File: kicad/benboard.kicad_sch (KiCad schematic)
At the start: 58 parts, among them J1 USB_C_Receptacle_USB2.0, SW1 SW_Push, U1 nRF52840, U2 BQ24075RGT, Y1 32MHz, Y2 32.768kHz

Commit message: more cad files as well as readme
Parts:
- added J2: ~, symbol vik:vik-keyboard-connector
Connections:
- net GND: now also J2.2 (GND)
- net VBUS: now also J2.6 (5V)
- net VDD_NRF: now also J2.1 (3V3)
- no-connect marks 6 -> 7
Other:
- note added: "VIK"
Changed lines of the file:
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@@
   (no_connect (at 270.51 73.66))
   (no_connect (at 64.77 77.47))
+  (no_connect (at 177.8 190.5))
   (no_connect (at 171.45 62.23))
   (wire (pts (xy 116.84 181.61) (xy 115.57 181.61))
@@
     (stroke (width 0) (type default))
   )
+  (wire (pts (xy 177.8 182.88) (xy 163.83 182.88))
+    (stroke (width 0) (type default))
+  )
   (wire (pts (xy 116.84 176.53) (xy 115.57 176.53))
     (stroke (width 0) (type default))
@@
     (stroke (width 0) (type default))
   )
+  (wire (pts (xy 176.53 193.04) (xy 177.8 193.04))
+    (stroke (width 0) (type default))
+  )
   (wire (pts (xy 224.79 147.32) (xy 223.52 147.32))
     (stroke (width 0) (type default))
@@
     (stroke (width 0) (type default))
   )
+  (wire (pts (xy 176.53 180.34) (xy 177.8 180.34))
+    (stroke (width 0) (type default))
+  )
   (wire (pts (xy 100.33 35.56) (xy 100.33 36.83))
     (stroke (width 0) (type default))
@@
     (stroke (width 0) (type default))
   )
+  (wire (pts (xy 163.83 182.88) (xy 163.83 184.15))
+    (stroke (width 0) (type default))
+  )
   (wire (pts (xy 271.78 62.23) (xy 271.78 63.5))
     (stroke (width 0) (type default))
@@
   )
   (rectangle (start 149.86 12.7) (end 236.22 93.98)
+    (stroke (width 0) (type default))
+    (fill (type none))
+  )
+  (rectangle (start 149.86 160.02) (end 205.74 229.87)
     (stroke (width 0) (type default))
     (fill (type none))
@@
   )
   (text "Battery Charging\n" (at 189.23 17.78 0)
+    (effects (font (size 3 3)) (justify right bottom))
+  )
+  (text "VIK" (at 158.75 166.37 0)
     (effects (font (size 3 3)) (justify right bottom))
   )
@@
     )
   )
+  (global_label "VDD_NRF" (shape input) (at 176.53 180.34 180) (fields_autoplaced)
+    (effects (font (size 1.27 1.27)) (justify right))
+    (property "Intersheetrefs" "${INTERSHEET_REFS}" (at 165.2595 180.34 0)
+      (effects (font (size 1.27 1.27)) (justify right) hide)
+    )
+  )
   (global_label "SW20" (shape input) (at 116.84 173.99 0) (fields_autoplaced)
     (effects (font (size 1.27 1.27)) (justify left))
@@
     )
   )
+  (global_label "VBUS" (shape input) (at 176.53 193.04 180) (fields_autoplaced)
+    (effects (font (size 1.27 1.27)) (justify right))
+    (property "Intersheetrefs" "${INTERSHEET_REFS}" (at 168.6462 193.04 0)
+      (effects (font (size 1.27 1.27)) (justify right) hide)
+    )
+  )
   (global_label "VDD_NRF" (shape input) (at 82.55 53.34 90) (fields_autoplaced)
     (effects (font (size 1.27 1.27)) (justify left))
@@
         (path "/b2065370-6f3a-4205-b26a-a9c2368077cd"
           (reference "SW4") (unit 1)
+        )
+      )
+    )
+  )
+  (symbol (lib_id "vik:vik-keyboard-connector") (at 177.8 194.31 0) (unit 1)
+    (in_bom yes) (on_board yes) (dnp no) (fields_autoplaced)
+    (property "Reference" "J2" (at 181.61 194.31 0)
+      (effects (font (size 1.27 1.27)) (justify left))
+    )
+    (property "Value" "~" (at 177.8 187.96 0)
+      (effects (font (size 1.27 1.27)))
+    )
+    (property "Footprint" "" (at 177.8 187.96 0)
+      (effects (font (size 1.27 1.27)) hide)
+    )
+    (property "Datasheet" "" (at 177.8 187.96 0)
+      (effects (font (size 1.27 1.27)) hide)
+    )
+    (pin "1")
+    (pin "10")
+    (pin "11")
+    (pin "12")
+    (pin "2")
+    (pin "3")
+    (pin "4")
+    (pin "5")
+    (pin "6")
+    (pin "7")
+    (pin "8")
+    (pin "9")
+    (instances
+      (project "benboard"
+        (path "/b2065370-6f3a-4205-b26a-a9c2368077cd"
+          (reference "J2") (unit 1)
         )
       )
@@
         )
       )
+    )
+  )
+  (symbol (lib_id "power:GND") (at 163.83 184.15 0) (unit 1)
+    (in_bom yes) (on_board yes) (dnp no)
+    (property "Reference" "#PWR045" (at 163.83 190.5 0)
+      (effects (font (size 1.27 1.27)) hide)
+    )
+    (property "Value" "GND" (at 163.83 187.96 0)
+      (effects (font (size 1.27 1.27)))
+    )
+    (property "Footprint" "" (at 163.83 184.15 0)
+      (effects (font (size 1.27 1.27)) hide)
+    )
+    (property "Datasheet" "" (at 163.83 184.15 0)
+      (effects (font (size 1.27 1.27)) hide)
+    )
+    (pin "1")
+    (instances
+      (project "benboard"
+        (path "/b2065370-6f3a-4205-b26a-a9c2368077cd"
+          (reference "#PWR045") (unit 1)
+        )
+      )

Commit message: add vik
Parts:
- C1: footprint Capacitor_SMD:C_0603_1608Metric -> Connector_FFC-FPC:TE_1-84953-2_1x12-1MP_P1.0mm_Horizontal
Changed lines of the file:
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@@
       (effects (font (size 1.27 1.27)))
     )
-    (property "Footprint" "Capacitor_SMD:C_0603_1608Metric" (at 99.06 34.5948 0)
+    (property "Footprint" "Connector_FFC-FPC:TE_1-84953-2_1x12-1MP_P1.0mm_Horizontal" (at 99.06 34.5948 0)
       (effects (font (size 1.27 1.27)) hide)
     )

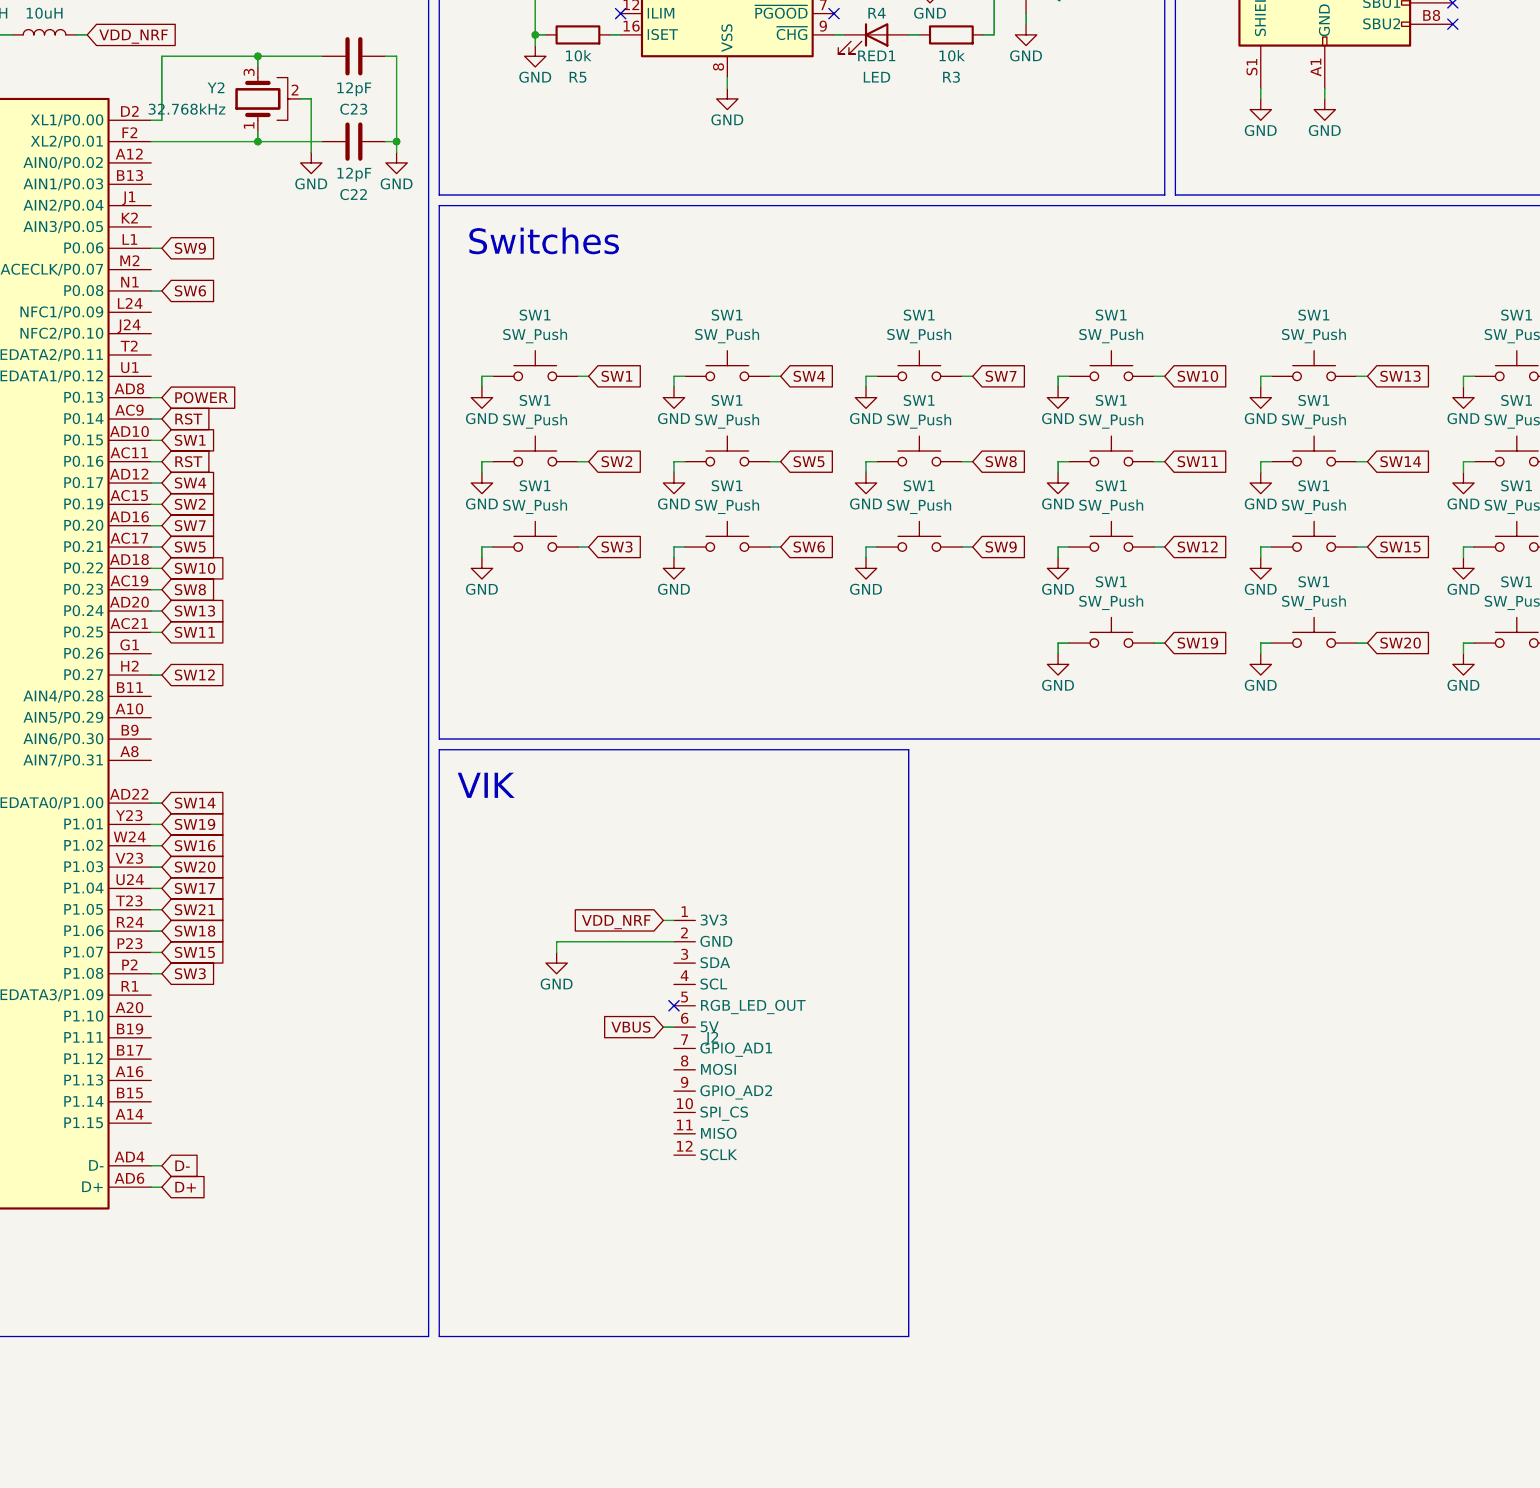
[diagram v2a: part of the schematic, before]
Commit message: add vik and SWD
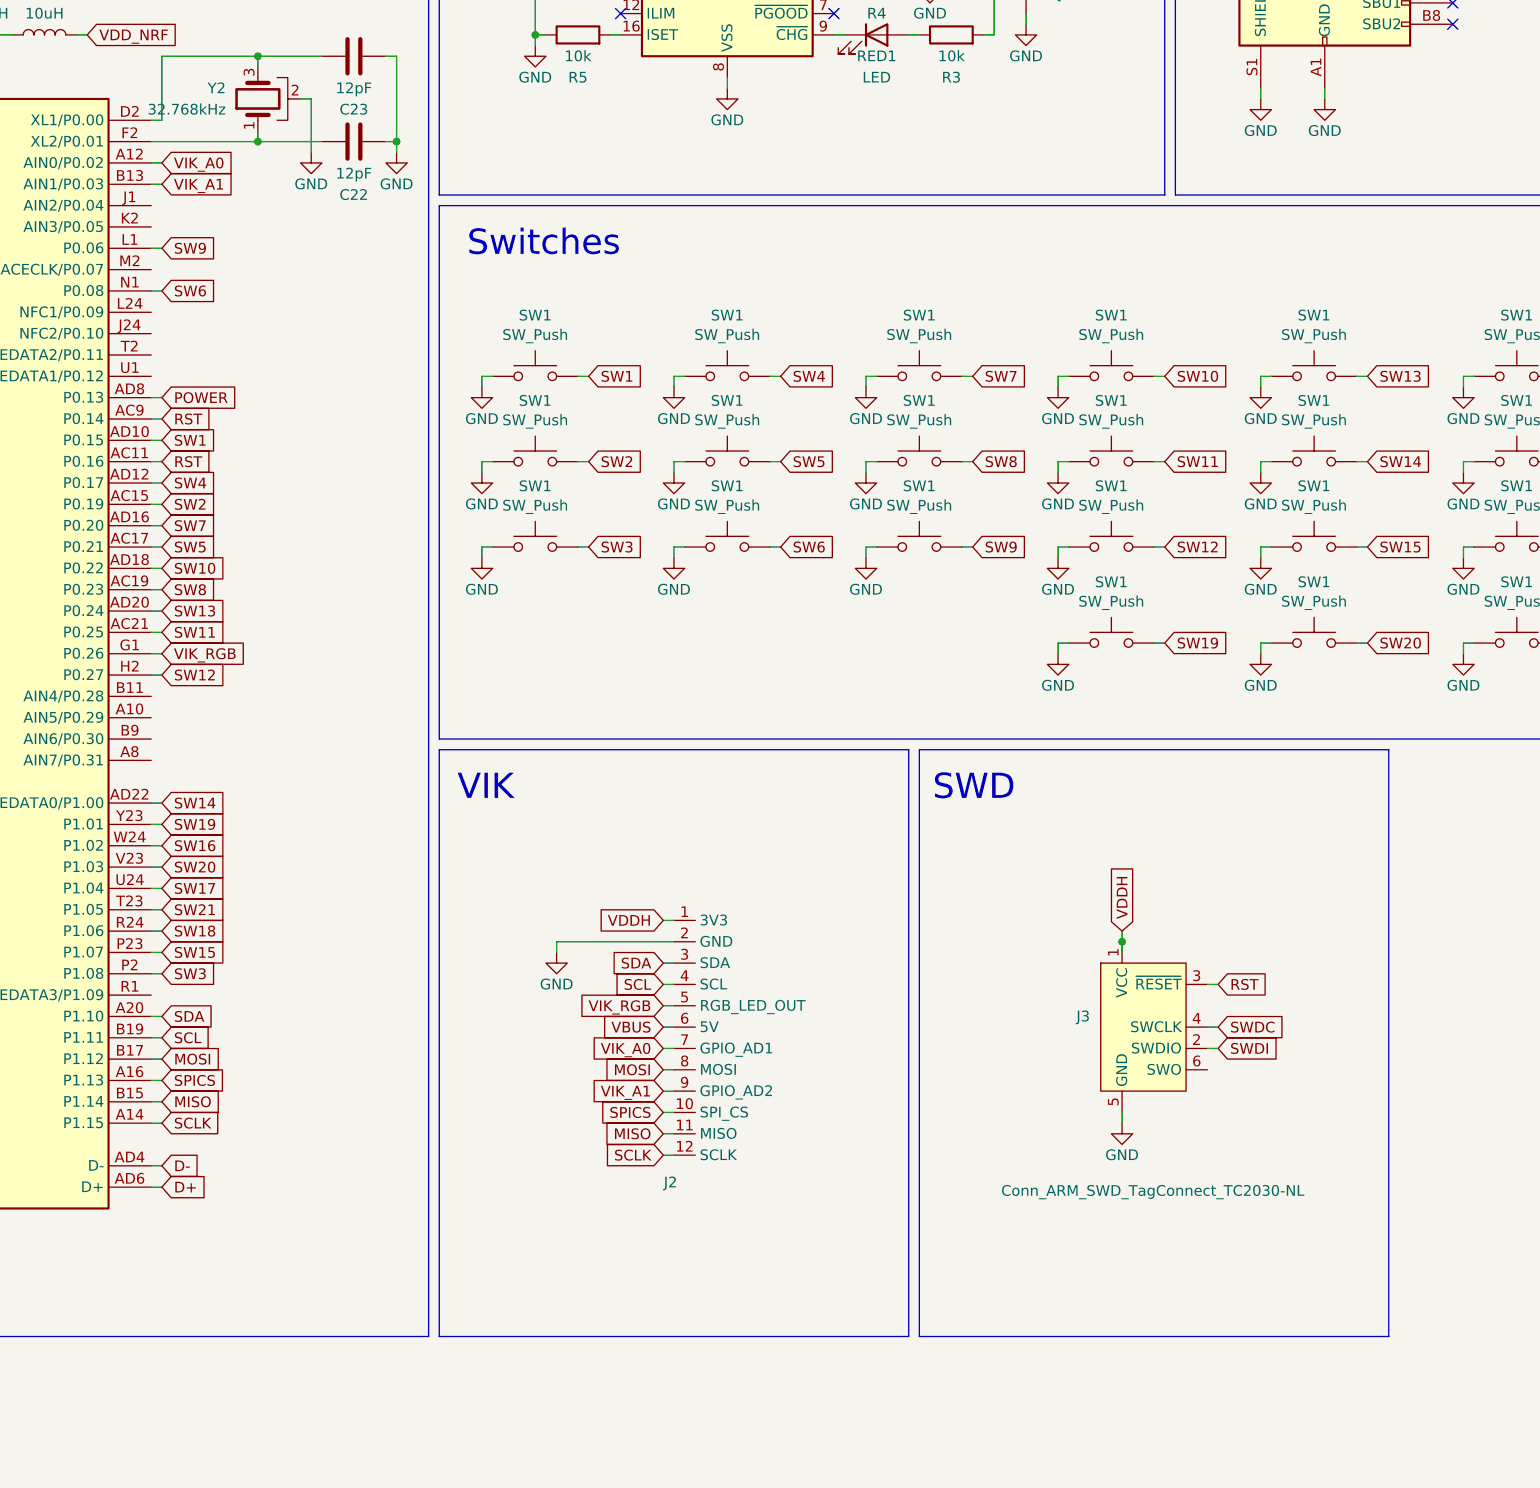
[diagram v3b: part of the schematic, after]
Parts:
- added J3: Conn_ARM_SWD_TagConnect_TC2030-NL, Connector:Tag-Connect_TC2030-IDC-NL_2x03_P1.27mm_Vertical, symbol Connector:Conn_ARM_SWD_TagConnect_TC2030-NL
- J2: footprint (none) -> vik:vik-keyboard-connector-horizontal
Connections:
- net GND: now also J3.5 (GND)
- net RST: now also J3.3 (~{RESET})
- net SWDC: now also J3.4 (SWCLK)
- net SWDI: now also J3.2 (SWDIO)
- net VDDH: now also J2.1 (3V3), J3.1 (VCC)
- net VDD_NRF: no longer J2.1 (3V3)
- net SPICS: now reaches J2.10 (SPI_CS)
- net SPICS: now also U1.A16 (P1.13)
- net MISO: now reaches J2.11 (MISO)
- net MISO: now also U1.B15 (P1.14)
- net SCLK: now reaches J2.12 (SCLK)
- net SCLK: now also U1.A14 (P1.15)
- net SDA: now reaches J2.3 (SDA)
- net SDA: now also U1.A20 (P1.10)
- net SCL: now reaches J2.4 (SCL)
- net SCL: now also U1.B19 (P1.11)
- net VIK_RGB: now reaches J2.5 (RGB_LED_OUT)
- net VIK_RGB: now also U1.G1 (P0.26)
- net VIK_A0: now reaches J2.7 (GPIO_AD1)
- net VIK_A0: now also U1.A12 (AIN0/P0.02)
- net MOSI: now reaches J2.8 (MOSI)
- net MOSI: now also U1.B17 (P1.12)
- net VIK_A1: now reaches J2.9 (GPIO_AD2)
- net VIK_A1: now also U1.B13 (AIN1/P0.03)
- no-connect marks 7 -> 6
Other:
- note added: "SWD"
